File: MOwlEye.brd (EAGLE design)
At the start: 160 x 100 mm, 38 parts

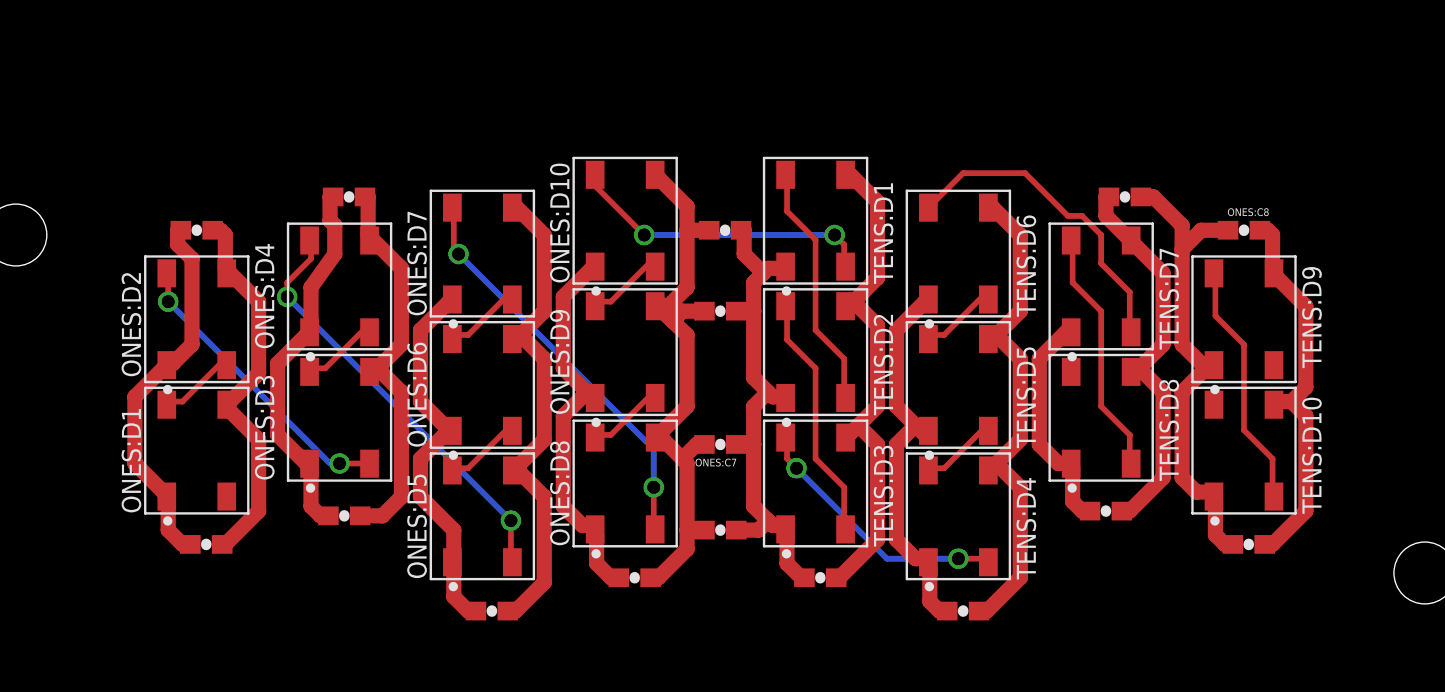
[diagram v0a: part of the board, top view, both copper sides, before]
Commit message: Use Import to make a two eye schematic, add power regulator, basic routing.
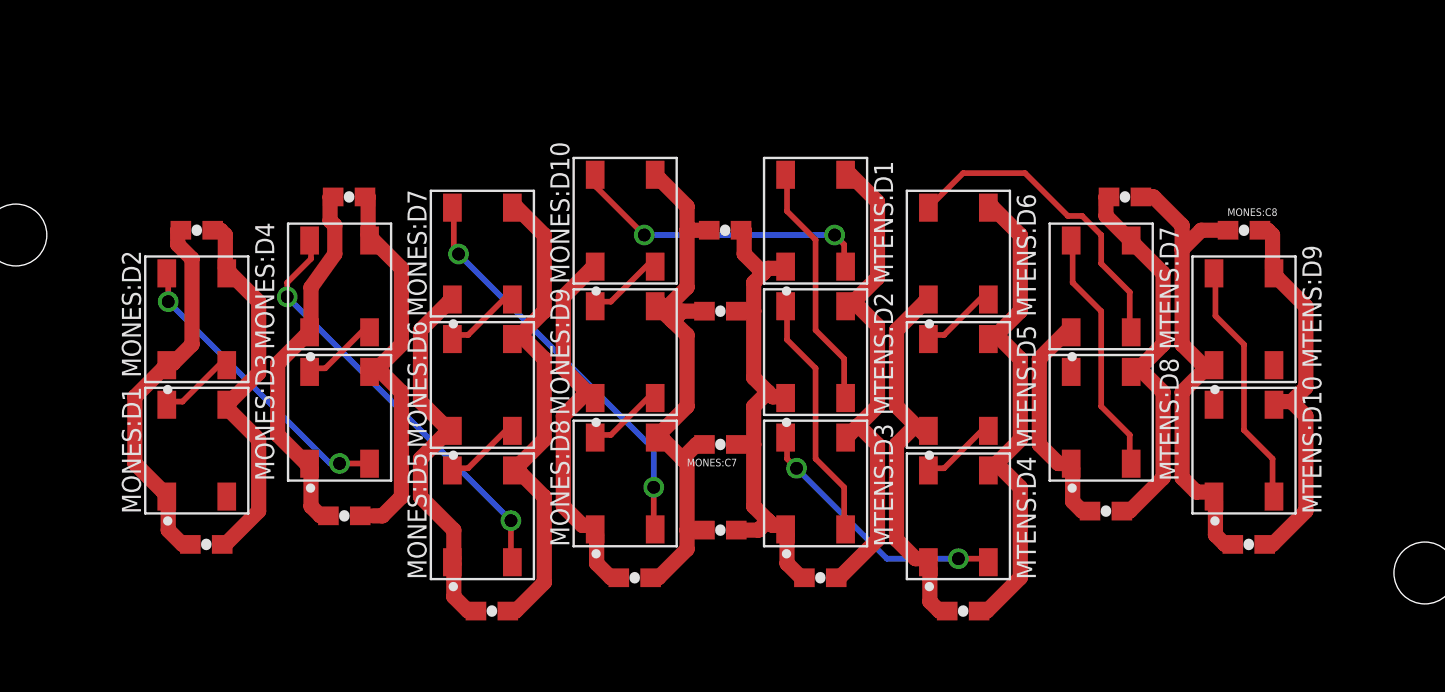
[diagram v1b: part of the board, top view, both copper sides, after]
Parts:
- renumbered ONES:C1 to MONES:C1, ONES:C2 to MONES:C2, ONES:C3 to MONES:C3, ONES:C4 to MONES:C4, ONES:C5 to MONES:C5, ONES:C6 to MONES:C6, ONES:C7 to MONES:C7, ONES:C8 to MONES:C8, ONES:D1 to MONES:D1, ONES:D10 to MONES:D10, ONES:D2 to MONES:D2, ONES:D3 to MONES:D3, ONES:D4 to MONES:D4, ONES:D5 to MONES:D5, ONES:D6 to MONES:D6, ONES:D7 to MONES:D7, ONES:D8 to MONES:D8, ONES:D9 to MONES:D9, TENS:C1 to MTENS:C1, TENS:C2 to MTENS:C2, TENS:C3 to MTENS:C3, TENS:C4 to MTENS:C4, TENS:C5 to MTENS:C5, TENS:C6 to MTENS:C6, TENS:C7 to MTENS:C7, TENS:C8 to MTENS:C8, TENS:D1 to MTENS:D1, TENS:D10 to MTENS:D10, TENS:D2 to MTENS:D2, TENS:D3 to MTENS:D3, TENS:D4 to MTENS:D4, TENS:D5 to MTENS:D5, TENS:D6 to MTENS:D6, TENS:D7 to MTENS:D7, TENS:D8 to MTENS:D8, TENS:D9 to MTENS:D9
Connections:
- net ONES:N$1 renamed MONES:N$1
- net ONES:N$10 renamed MONES:N$10
- net ONES:N$12 renamed MONES:N$12
- net ONES:N$13 renamed MONES:N$13
- net ONES:N$15 renamed MONES:N$15
- net ONES:N$5 renamed MONES:N$5
- net ONES:N$6 renamed MONES:N$6
- net ONES:N$7 renamed MONES:N$7
- net ONES:N$9 renamed MONES:N$9
- net TENS:N$1 renamed MTENS:N$1
- net TENS:N$10 renamed MTENS:N$10
- net TENS:N$12 renamed MTENS:N$12
- net TENS:N$13 renamed MTENS:N$13
- net TENS:N$15 renamed MTENS:N$15
- net TENS:N$5 renamed MTENS:N$5
- net TENS:N$6 renamed MTENS:N$6
- net TENS:N$7 renamed MTENS:N$7
- net TENS:N$9 renamed MTENS:N$9
